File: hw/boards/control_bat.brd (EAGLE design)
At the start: 100.1 x 30.5 mm, 18 parts, among them U1 579-MCP1703T-3002ECB, U2 771-LPC824M201JDH20J, U3 888-XB24CZ7PIS-004

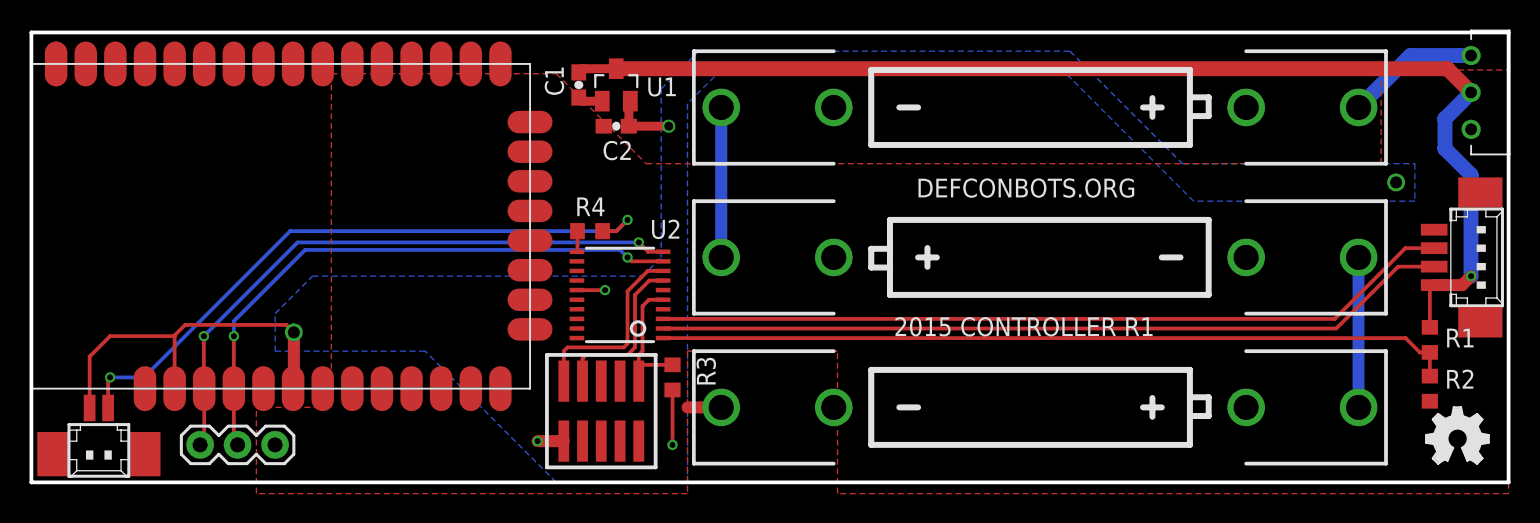
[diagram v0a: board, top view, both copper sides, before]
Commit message: Fix length to be 10cm
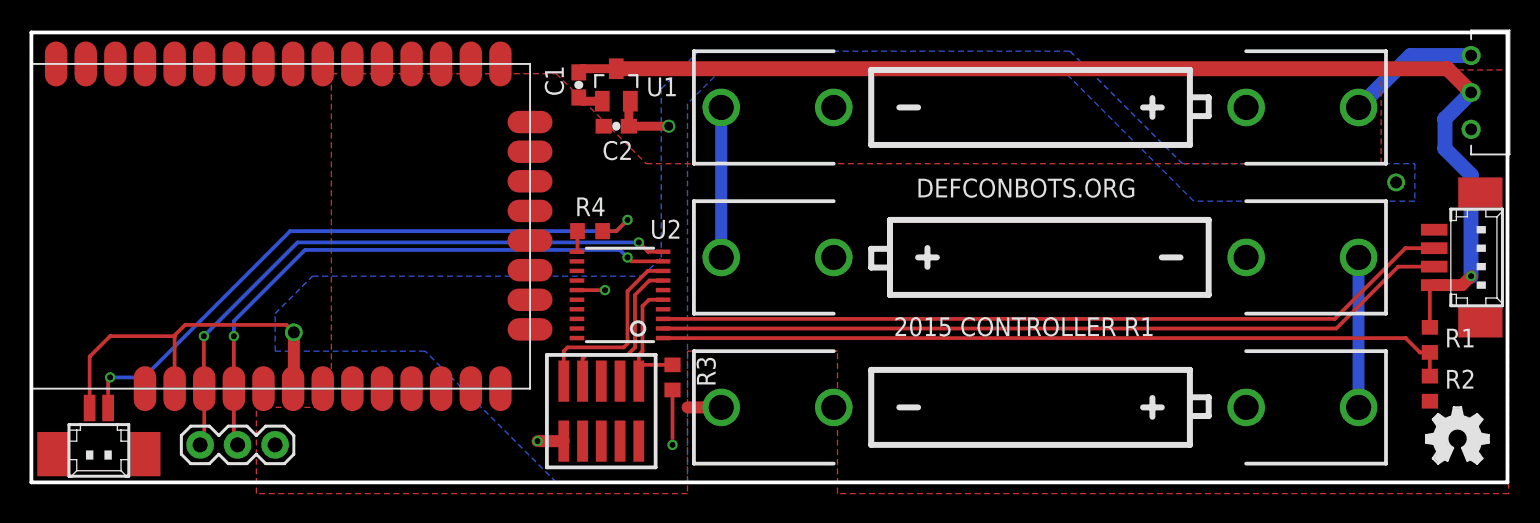
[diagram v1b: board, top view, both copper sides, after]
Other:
- board size 100.1 x 30.5 mm -> 100 x 30.5 mm
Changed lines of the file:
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@@
 <setting verticaltext="up"/>
 </settings>
-<grid distance="0.05" unitdist="inch" unit="inch" style="lines" multiple="1" display="yes" altdistance="0.01" altunitdist="inch" altunit="inch"/>
+<grid distance="1" unitdist="mm" unit="mm" style="lines" multiple="1" display="yes" altdistance="0.01" altunitdist="inch" altunit="inch"/>
 <layers>
 <layer number="1" name="Top" color="4" fill="1" visible="yes" active="yes"/>
@@
 <board>
 <plain>
-<wire x1="0" y1="0" x2="100.076" y2="0" width="0.254" layer="20"/>
-<wire x1="100.076" y1="0" x2="100.076" y2="30.48" width="0.254" layer="20"/>
-<wire x1="100.076" y1="30.48" x2="0" y2="30.48" width="0.254" layer="20"/>
+<wire x1="0" y1="0" x2="100" y2="0" width="0.254" layer="20"/>
+<wire x1="100" y1="0" x2="100" y2="30.48" width="0.254" layer="20"/>
+<wire x1="100" y1="30.48" x2="0" y2="30.48" width="0.254" layer="20"/>
 <wire x1="0" y1="30.48" x2="0" y2="0" width="0.254" layer="20"/>
 <text x="59.944" y="19.304" size="1.27" layer="21" font="vector" ratio="10">DEFCONBOTS.ORG</text>

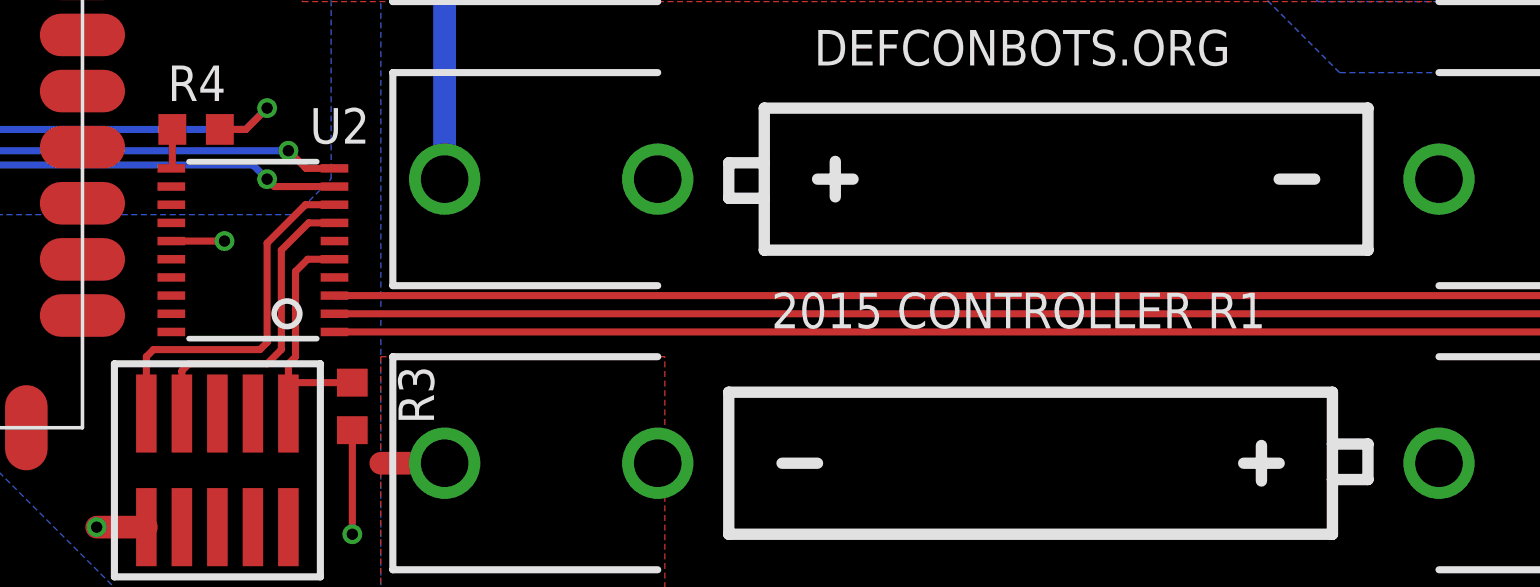
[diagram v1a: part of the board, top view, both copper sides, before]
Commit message: Fix adc.
There is no internal reference so I needed to connect the VREFP/VREFN pints to VCC/GND. Added init code to read single adc samples when the voltage-read command is passed.
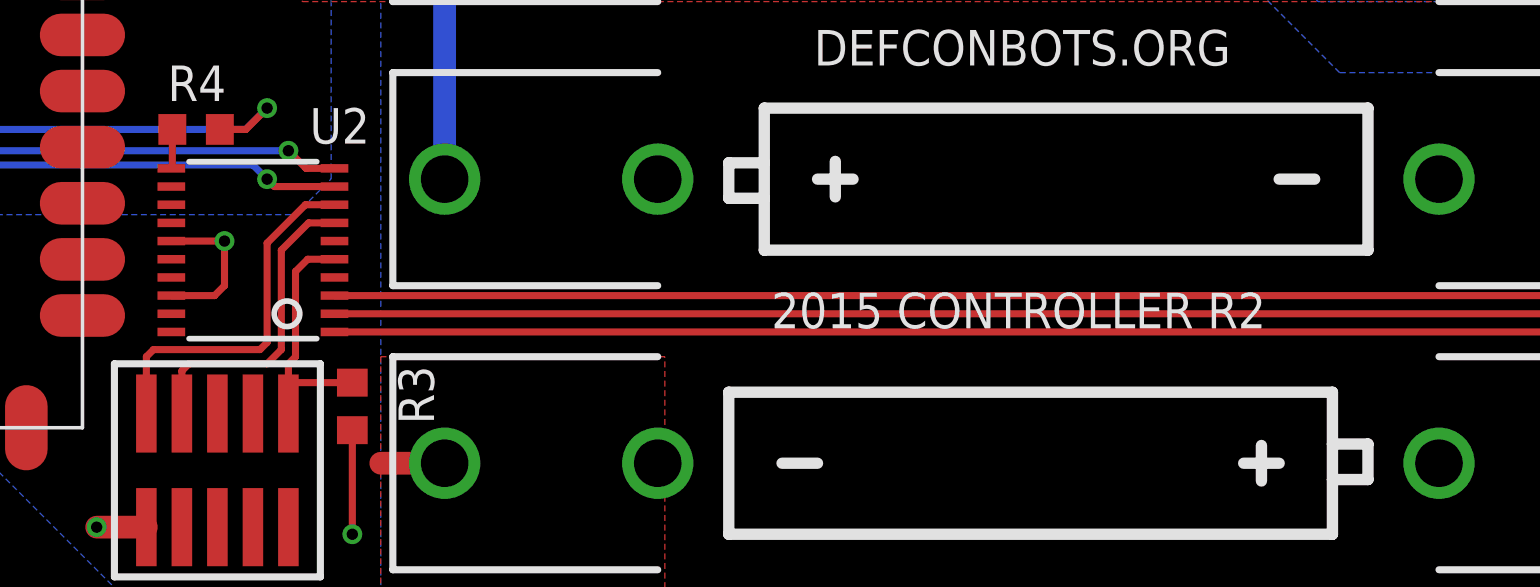
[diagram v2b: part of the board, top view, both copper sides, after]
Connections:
- net +3V3: now also U2.18
- net GND: now also U2.17
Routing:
- net +3V3: track 37.7 -> 41.3 mm
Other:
- board text added: "2015 CONTROLLER R2"
- board text removed: "2015 CONTROLLER R1"
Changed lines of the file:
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@@
 <setting verticaltext="up"/>
 </settings>
-<grid distance="1" unitdist="mm" unit="mm" style="lines" multiple="1" display="yes" altdistance="0.01" altunitdist="inch" altunit="inch"/>
+<grid distance="0.01" unitdist="inch" unit="inch" style="lines" multiple="1" display="yes" altdistance="0.01" altunitdist="inch" altunit="inch"/>
 <layers>
 <layer number="1" name="Top" color="4" fill="1" visible="yes" active="yes"/>
@@
 <wire x1="0" y1="30.48" x2="0" y2="0" width="0.254" layer="20"/>
 <text x="59.944" y="19.304" size="1.27" layer="21" font="vector" ratio="10">DEFCONBOTS.ORG</text>
-<text x="58.42" y="9.906" size="1.27" layer="21" font="vector" ratio="10">2015 CONTROLLER R1</text>
+<text x="58.42" y="9.906" size="1.27" layer="21" font="vector" ratio="10">2015 CONTROLLER R2</text>
 </plain>
 <attributes>
@@
 <wire x1="37.084" y1="26.074" x2="37.334" y2="25.824" width="0.6096" layer="1"/>
 <wire x1="37.334" y1="25.824" x2="38.674" y2="25.824" width="0.6096" layer="1"/>
+<contactref element="U2" pad="17"/>
 </signal>
 <signal name="+3V3">
@@
 <wire x1="40.474" y1="24.13" x2="43.18" y2="24.13" width="0.6096" layer="1"/>
 <via x="43.18" y="24.13" extent="1-16" drill="0.6"/>
+<contactref element="U2" pad="18"/>
+<wire x1="36.9602" y1="11.075" x2="38.507" y2="11.075" width="0.254" layer="1"/>
+<wire x1="38.507" y1="11.075" x2="38.862" y2="11.43" width="0.254" layer="1"/>
+<wire x1="38.862" y1="11.43" x2="38.862" y2="13.025" width="0.254" layer="1"/>
 </signal>
 <signal name="VIN">

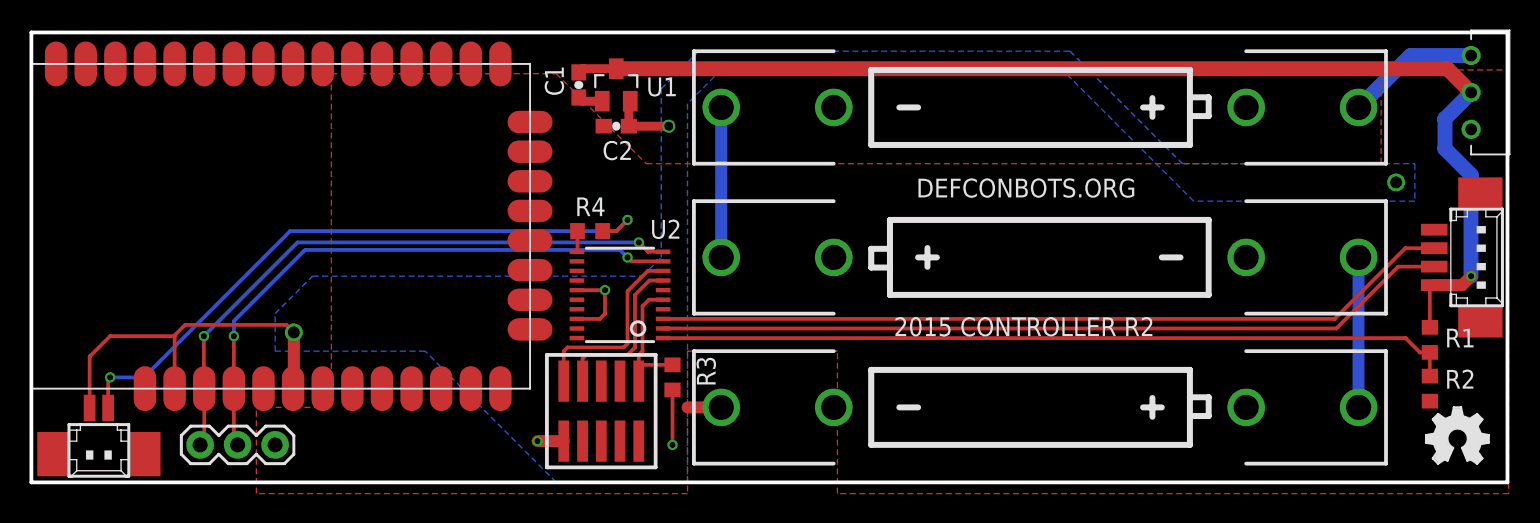
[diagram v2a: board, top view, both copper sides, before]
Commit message: Final fixes to the controller board.
This board will probably never be fabbed but I'm documenting the fixes made to hardware here for future reference.
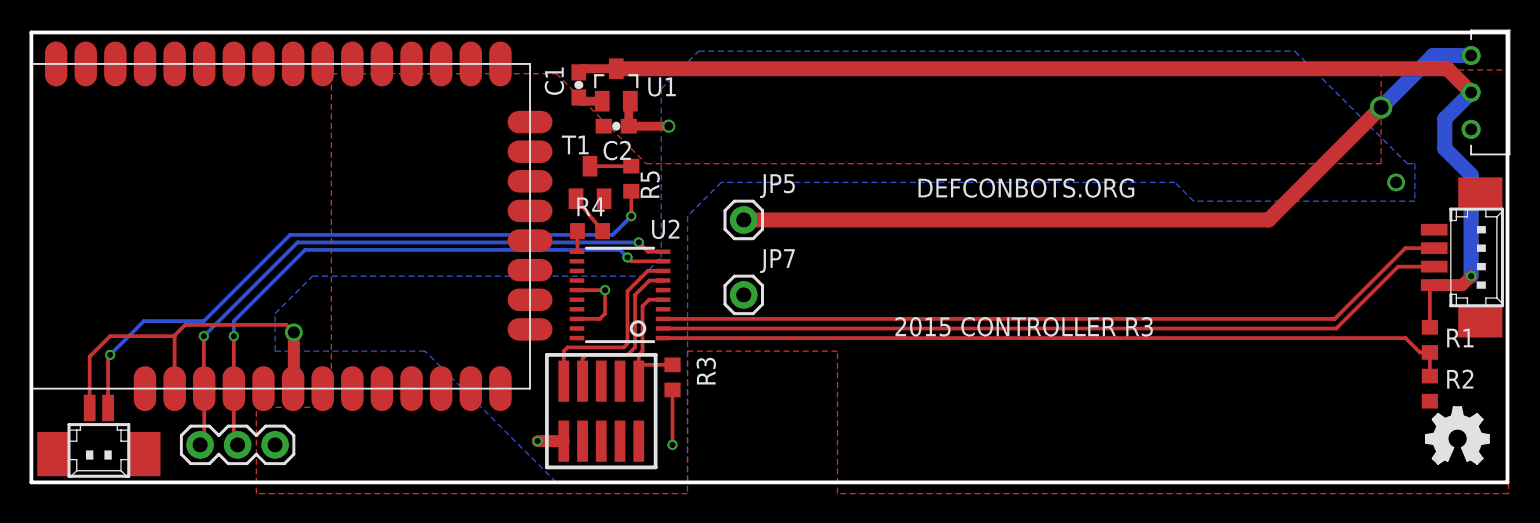
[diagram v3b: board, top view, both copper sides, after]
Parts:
- removed BAT1, BAT2, BAT3: 534-082, SparkFun-Electromechanical:BATTERY-AAA-KIT
- added JP5, JP7: M01PTH, SparkFun-Connectors:1X01
- added R5: 71-CRCW0603-5.6-E3, rcl:R0603
- added T1: PMBT4401,215, transistor:SOT23-BEC
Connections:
- removed net N$2: BAT1.GND@1, BAT2.PWR@1
- removed net N$3: BAT1.PWR@1, S1.P$1
- new net N$5: R5.1, T1.C
- new net N$6: R4.2, T1.B
- net GND: now also JP7.1, T1.E; no longer BAT3.GND@1
- net N$1: now also JP5.1, S1.P$1; no longer BAT2.GND@1, BAT3.PWR@1
- net N$4: now also R5.2; no longer R4.2
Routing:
- net N$1: track 10.2 -> 53.9 mm, vias 0 -> 1
- net N$2: track 10.2 -> 0.00 mm
- net N$3: track 9.08 -> 0.00 mm
- net N$6: track 0.00 -> 2.84 mm
- net N$5: track 0.00 -> 2.79 mm
- net GND: track 3.98 -> 1.69 mm
- net N$4: track 43.6 -> 44.5 mm
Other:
- board text added: "2015 CONTROLLER R3"
- board text removed: "2015 CONTROLLER R2"
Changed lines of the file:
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@@
 <setting verticaltext="up"/>
 </settings>
-<grid distance="0.01" unitdist="inch" unit="inch" style="lines" multiple="1" display="yes" altdistance="0.01" altunitdist="inch" altunit="inch"/>
+<grid distance="0.1" unitdist="inch" unit="inch" style="lines" multiple="1" display="yes" altdistance="0.01" altunitdist="inch" altunit="inch"/>
 <layers>
 <layer number="1" name="Top" color="4" fill="1" visible="yes" active="yes"/>
@@
 <wire x1="0" y1="30.48" x2="0" y2="0" width="0.254" layer="20"/>
 <text x="59.944" y="19.304" size="1.27" layer="21" font="vector" ratio="10">DEFCONBOTS.ORG</text>
-<text x="58.42" y="9.906" size="1.27" layer="21" font="vector" ratio="10">2015 CONTROLLER R2</text>
+<text x="58.42" y="9.906" size="1.27" layer="21" font="vector" ratio="10">2015 CONTROLLER R3</text>
 </plain>
 <attributes>
@@
 </element>
 <element name="JP1" library="torpedo" package="FTSH-105-01-XXX-DV-K" value="FTSH-105-01-L" x="38.608" y="4.826" smashed="yes"/>
-<element name="BAT3" library="SparkFun-Electromechanical" package="BATTERY-AAA-KIT" value="534-082" x="68.326" y="5.08" smashed="yes" rot="R180">
-<attribute name="PROD_ID" value="BATT-08571" x="68.326" y="5.08" size="1.778" layer="27" rot="R180" display="off"/>
-</element>
 <element name="U3" library="xbee" package="XBEE-SMT" value="888-XB24CZ7PIS-004" x="33.782" y="6.35" smashed="yes" rot="R90"/>
-<element name="BAT2" library="SparkFun-Electromechanical" package="BATTERY-AAA-KIT" value="534-082" x="68.326" y="15.24" smashed="yes">
-<attribute name="PROD_ID" value="BATT-08571" x="68.326" y="15.24" size="1.778" layer="27" display="off"/>
-</element>
-<element name="BAT1" library="SparkFun-Electromechanical" package="BATTERY-AAA-KIT" value="534-082" x="68.326" y="25.4" smashed="yes" rot="R180">
-<attribute name="PROD_ID" value="BATT-08571" x="68.326" y="25.4" size="1.778" layer="27" rot="R180" display="off"/>
-</element>
 <element name="LOGO1" library="ohw-logo" package="OSHW_FILLX150_NOTEXT" value="OSHW_LOGO_FILLX0150-NT" x="94.488" y="1.27" smashed="yes"/>
 <element name="R1" library="rcl" package="R0603" value="71-CRCW0603-10K-E3" x="94.742" y="9.652" smashed="yes" rot="R90">
@@
 <attribute name="VALUE" x="7.072" y="6.04" size="1.27" layer="27" rot="R180"/>
 </element>
+<element name="T1" library="transistor" package="SOT23-BEC" value="PMBT4401,215" x="37.846" y="20.32"/>
+<element name="R5" library="rcl" package="R0603" value="71-CRCW0603-5.6-E3" x="40.64" y="20.574" rot="R270"/>
+<element name="JP5" library="SparkFun-Connectors" package="1X01" value="M01PTH" x="48.26" y="17.78"/>
+<element name="JP7" library="SparkFun-Connectors" package="1X01" value="M01PTH" x="48.26" y="12.7"/>
 </elements>
 <signals>
@@
 <contactref element="JP1" pad="3"/>
 <contactref element="U3" pad="13"/>
-<contactref element="BAT3" pad="GND@1"/>
 <contactref element="U3" pad="27"/>
 <contactref element="R2" pad="1"/>
@@
 <vertex x="20.32" y="5.08"/>
 </polygon>
-<wire x1="46.736" y1="5.08" x2="44.45" y2="5.08" width="0.8128" layer="1"/>
 <contactref element="JP4" pad="3"/>
 <contactref element="U2" pad="16"/>
@@
 <wire x1="37.334" y1="25.824" x2="38.674" y2="25.824" width="0.6096" layer="1"/>
 <contactref element="U2" pad="17"/>
+<contactref element="T1" pad="E"/>
+<contactref element="JP7" pad="1"/>
 </signal>
 <signal name="+3V3">
@@
 <vertex x="42.672" y="26.67"/>
 <vertex x="45.212" y="29.21"/>
-<vertex x="70.358" y="29.21"/>
-<vertex x="77.978" y="21.59"/>
+<vertex x="85.598" y="29.21"/>
+<vertex x="93.218" y="21.59"/>
 <vertex x="93.726" y="21.59"/>
 <vertex x="93.726" y="19.05"/>
 <vertex x="78.74" y="19.05"/>
-<vertex x="69.85" y="27.94"/>
-<vertex x="46.736" y="27.94"/>
-<vertex x="44.45" y="25.654"/>
+<vertex x="77.47" y="20.32"/>
+<vertex x="46.736" y="20.32"/>
+<vertex x="44.45" y="18.034"/>
 <vertex x="44.45" y="0"/>
 <vertex x="35.56" y="0"/>
@@
 <wire x1="42.7958" y1="11.075" x2="88.291" y2="11.075" width="0.254" layer="1"/>
 </signal>
-<signal name="N$1">
-<contactref element="BAT3" pad="PWR@1"/>
-<contactref element="BAT2" pad="GND@1"/>
-<wire x1="89.916" y1="15.24" x2="89.916" y2="5.08" width="0.8128" layer="16"/>
-</signal>
-<signal name="N$2">
-<contactref element="BAT2" pad="PWR@1"/>
-<contactref element="BAT1" pad="GND@1"/>
-<wire x1="46.736" y1="15.24" x2="46.736" y2="25.4" width="0.8128" layer="16"/>
-</signal>
 <signal name="RF_TX">
 <contactref element="U3" pad="4"/>
@@
 <wire x1="42.7958" y1="9.775" x2="93.095" y2="9.775" width="0.254" layer="1"/>
 </signal>
-<signal name="N$3">
-<contactref element="BAT1" pad="PWR@1"/>
-<contactref element="S1" pad="P$1"/>
-<wire x1="89.916" y1="25.4" x2="93.432" y2="28.916" width="1.016" layer="16"/>
-<wire x1="93.432" y1="28.916" x2="97.536" y2="28.916" width="1.016" layer="16"/>
-</signal>
-<signal name="N$4">
-<contactref element="R4" pad="2"/>
-<contactref element="JP2" pad="2"/>
-<wire x1="38.696" y1="17.018" x2="39.624" y2="17.018" width="0.254" layer="1"/>
-<wire x1="39.624" y1="17.018" x2="40.386" y2="17.78" width="0.254" layer="1"/>
-<via x="40.386" y="17.78" extent="1-16" drill="0.4064"/>
-<wire x1="40.386" y1="17.78" x2="39.624" y2="17.018" width="0.254" layer="16"/>
-<wire x1="39.624" y1="17.018" x2="17.526" y2="17.018" width="0.254" layer="16"/>
-<wire x1="17.526" y1="17.018" x2="7.62" y2="7.112" width="0.254" layer="16"/>
-<wire x1="7.62" y1="7.112" x2="5.334" y2="7.112" width="0.254" layer="16"/>
-<via x="5.334" y="7.112" extent="1-16" drill="0.4064"/>
-<wire x1="5.334" y1="7.112" x2="5.197" y2="6.975" width="0.254" layer="1"/>
-<wire x1="5.197" y1="6.975" x2="5.197" y2="5.04" width="0.254" layer="1"/>
-</signal>
 <signal name="IR">
 <contactref element="R4" pad="1"/>
@@
 <wire x1="36.996" y1="15.625" x2="36.996" y2="17.018" width="0.254" layer="1"/>
 </signal>
+<signal name="N$5">
+<contactref element="T1" pad="C"/>
+<contactref element="R5" pad="1"/>
+<wire x1="37.846" y1="21.42" x2="40.64" y2="21.424" width="0.254" layer="1"/>
+</signal>
+<signal name="N$4">
+<contactref element="R5" pad="2"/>
+<contactref element="JP2" pad="2"/>
+<wire x1="40.64" y1="19.724" x2="40.64" y2="18.034" width="0.254" layer="1"/>
+<via x="40.64" y="18.034" extent="1-16" drill="0.4064"/>
+<wire x1="40.64" y1="18.034" x2="39.37" y2="16.764" width="0.254" layer="16"/>
+<wire x1="39.37" y1="16.764" x2="17.526" y2="16.764" width="0.254" layer="16"/>
+<wire x1="17.526" y1="16.764" x2="11.684" y2="10.922" width="0.254" layer="16"/>
+<wire x1="11.684" y1="10.922" x2="7.62" y2="10.922" width="0.254" layer="16"/>
+<wire x1="7.62" y1="10.922" x2="5.334" y2="8.636" width="0.254" layer="16"/>
+<via x="5.334" y="8.636" extent="1-16" drill="0.4064"/>
+<wire x1="5.334" y1="8.636" x2="5.197" y2="8.499" width="0.254" layer="1"/>
+<wire x1="5.197" y1="8.499" x2="5.197" y2="5.04" width="0.254" layer="1"/>
+</signal>
+<signal name="N$6">
+<contactref element="R4" pad="2"/>
+<contactref element="T1" pad="B"/>
+<wire x1="38.696" y1="17.018" x2="36.896" y2="19.22" width="0.254" layer="1"/>
+</signal>
+<signal name="N$1">
+<contactref element="JP5" pad="1"/>
+<contactref element="S1" pad="P$1"/>
+<wire x1="48.26" y1="17.78" x2="83.82" y2="17.78" width="1.016" layer="1"/>
+<wire x1="83.82" y1="17.78" x2="91.44" y2="25.4" width="1.016" layer="1"/>
+<via x="91.44" y="25.4" extent="1-16" drill="1.016"/>
+<wire x1="91.44" y1="25.4" x2="94.956" y2="28.916" width="1.016" layer="16"/>
+<wire x1="94.956" y1="28.916" x2="97.536" y2="28.916" width="1.016" layer="16"/>
+</signal>
 </signals>
